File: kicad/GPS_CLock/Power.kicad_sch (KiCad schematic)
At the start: 50 parts, among them J201 USB_C_2.0, J202 BATT, Q201 PMPB17EP, Q202 PMPB17EP, U201 LP5912-3.3DRV, U202 STUSB4500QTR, U203 BQ25892, U204 TPS62827DMQ, U205 TPS62827DMQ

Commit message: updated pcb
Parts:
- removed J202: BATT, symbol Connector_Generic:Conn_01x02
- added BT201, BT202, BT203: Lipo, symbol Device:Battery_Cell
- C203, C205, C206, C212: footprint (none) -> Capacitor_SMD:C_0402_1005Metric
- C208, C209, C217, C218, C219, C221: footprint Capacitor_SMD:C_0402_1005Metric -> Capacitor_SMD:C_0603_1608Metric
- D201: footprint (none) -> Diode_SMD:D_SOD-323
- L201, L202: footprint Inductor_SMD:L_0805_2012Metric -> clock:L_DFE201610
- L203: footprint clock:Bourns_SRP2512 -> Inductor_SMD:L_Vishay_IHLP-2020
- Q201, Q202: footprint (none) -> clock:NXP_DFN6_2.0x2.0mm 2xEp
- R205: footprint (none) -> Resistor_SMD:R_0402_1005Metric
- U203: footprint (none) -> Package_DFN_QFN:Texas_S-PWQFN-N24_EP2.7x2.7mm
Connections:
- net +BATT: now also BT201.1 (+), BT202.1 (+), BT203.1 (+)
- net Earth: now also BT201.2 (-), BT202.2 (-), BT203.2 (-)
- net VBUS: now reaches D201.2 (A), J201.A4 (VBUS), J201.A9 (VBUS), J201.B4 (VBUS), J201.B9 (VBUS), Q201.1 (D), Q201.2 (D), Q201.5 (D), Q201.6 (D), Q201.7 (D), R201.1
- net VBUS_SNK: now reaches C207.1, C210.1, Q202.1 (D), Q202.2 (D), Q202.5 (D), Q202.6 (D), Q202.7 (D), U203.1 (VBUS)
- net PD_SCL: now reaches U202.7 (SCL)
- net PD_SDA: now reaches U202.8 (SDA)

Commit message: update pcb
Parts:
- C201, C220: footprint Capacitor_SMD:C_0402_1005Metric -> Capacitor_SMD:C_0603_1608Metric
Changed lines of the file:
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@@
       (effects (font (size 1.27 1.27)) (justify left))
     )
-    (property "Footprint" "Capacitor_SMD:C_0402_1005Metric" (id 2) (at 71.12 140.97 0)
+    (property "Footprint" "Capacitor_SMD:C_0603_1608Metric" (id 2) (at 71.12 140.97 0)
       (effects (font (size 1.27 1.27)) hide)
     )
@@
       (effects (font (size 1.27 1.27)) (justify left))
     )
-    (property "Footprint" "Capacitor_SMD:C_0402_1005Metric" (id 2) (at 228.6 138.43 0)
-      (effects (font (size 1.27 1.27)) hide)
-    )
+    (property "Footprint" "Capacitor_SMD:C_0603_1608Metric" (id 2) (at 228.6 138.43 0)
+      (effects (font (size 1.27 1.27)) hide)
+    )

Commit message: update pcb
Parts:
- added JP201, JP202: Jumper_2_Bridged, Connector_PinHeader_2.54mm:PinHeader_1x02_P2.54mm_Horizontal, symbol Jumper:Jumper_2_Bridged
- added R217, R218: 50, Resistor_SMD:R_1206_3216Metric, symbol Device:R_Small
- BT201, BT202, BT203: footprint (none) -> Connector_JST:JST_PH_S2B-PH-K_1x02_P2.00mm_Horizontal
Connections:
- net +BATT: now also JP201.2 (B), R217.1; no longer BT202.1 (+), BT203.1 (+)
- new net: BT202.1 (+), JP201.1 (A), JP202.2 (B), R217.2, R218.1
- new net: BT203.1 (+), JP202.1 (A), R218.2
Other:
- moved on the sheet: BT201, BT202, BT203

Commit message: update pcb
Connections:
- net PD_INT: now reaches U202.19 (ALERT)
- no-connect marks 13 -> 12

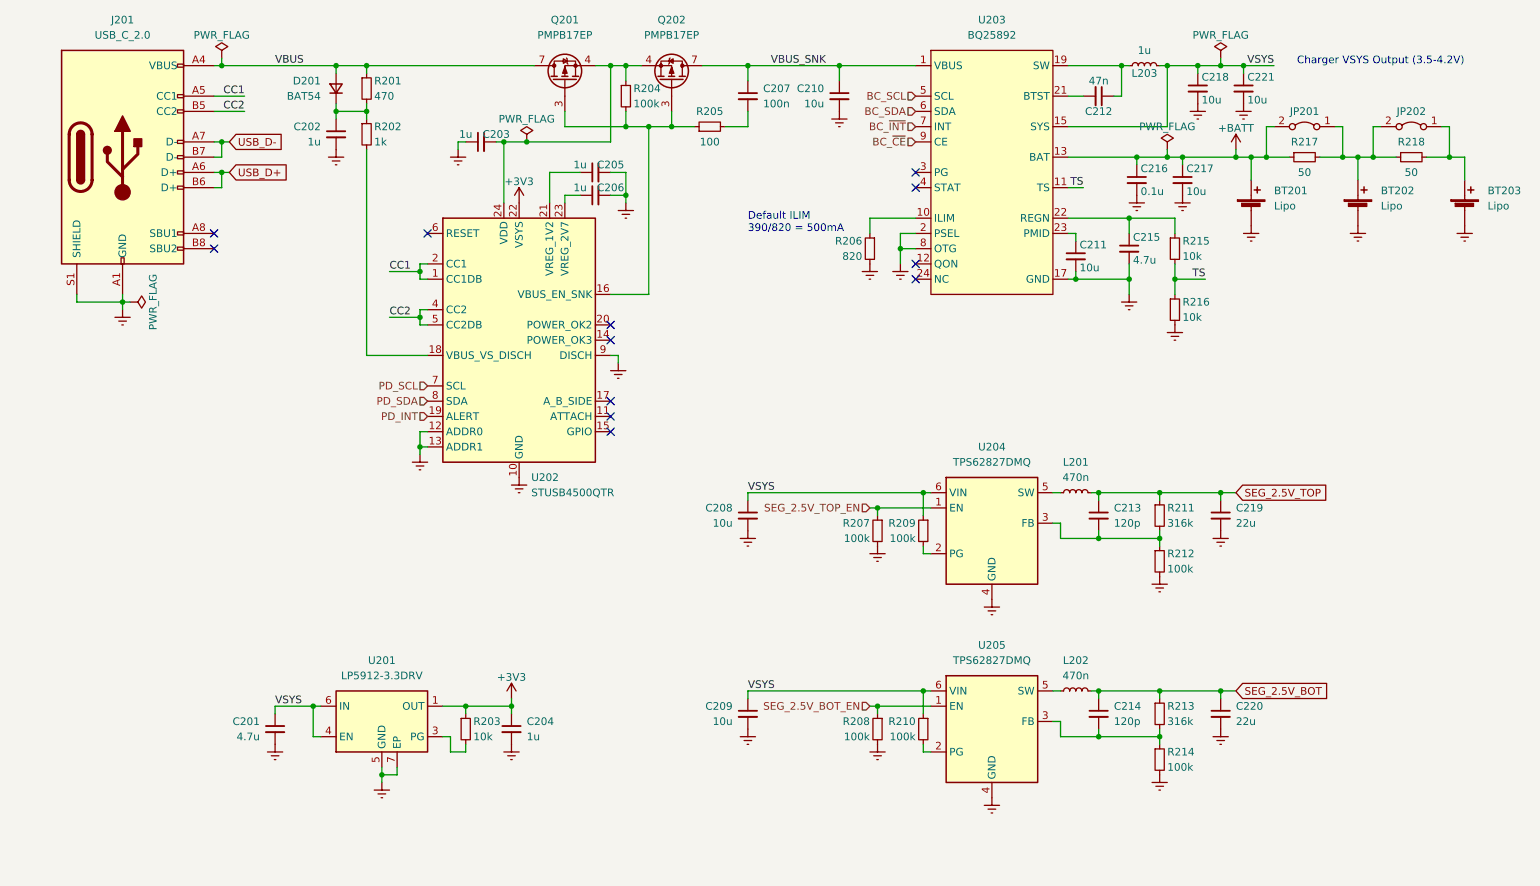
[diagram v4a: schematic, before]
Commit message: add quickcharge 3.0 capability
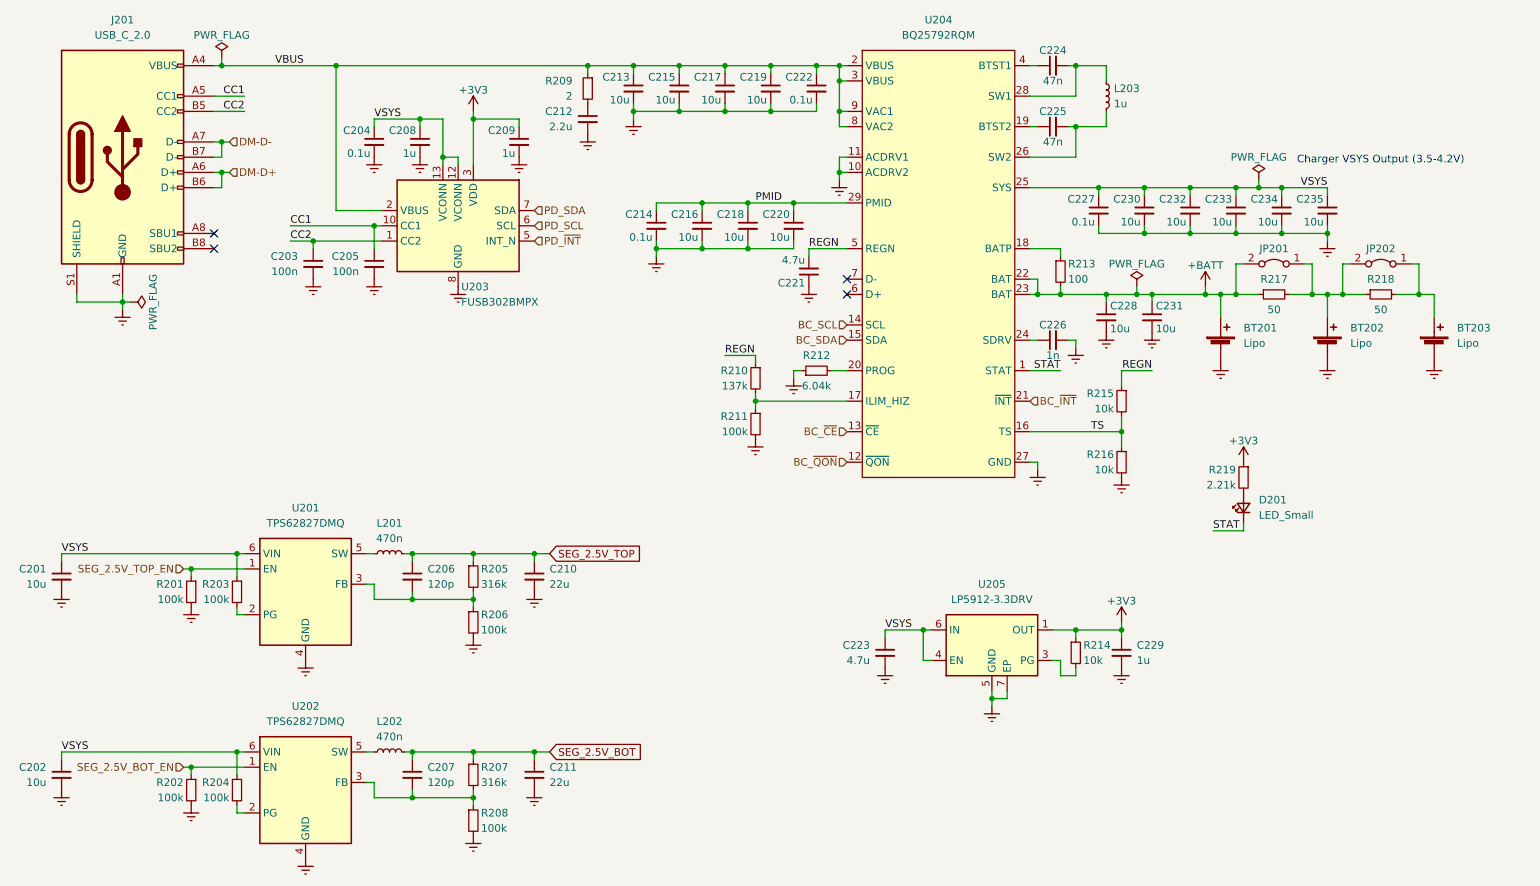
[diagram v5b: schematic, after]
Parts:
- removed C202, C206: 1u, Capacitor_SMD:C_0402_1005Metric, symbol Device:C_Small
- removed C207: 100n, Capacitor_SMD:C_0402_1005Metric, symbol Device:C_Small
- removed C211: 10u, Capacitor_SMD:C_0402_1005Metric, symbol Device:C_Small
- removed D201: BAT54, Diode_SMD:D_SOD-323, symbol Device:D_Small
- removed Q201, Q202: PMPB17EP, clock:NXP_DFN6_2.0x2.0mm 2xEp, symbol Clock:PMPB17EP
- removed R201: 470, Resistor_SMD:R_0402_1005Metric, symbol Device:R_Small
- removed R202: 1k, Resistor_SMD:R_0402_1005Metric, symbol Device:R_Small
- removed R204: 100k, Resistor_SMD:R_0402_1005Metric, symbol Device:R_Small
- removed R205: 100, Resistor_SMD:R_0402_1005Metric, symbol Device:R_Small
- removed U202: STUSB4500QTR, Package_DFN_QFN:QFN-24-1EP_4x4mm_P0.5mm_EP2.7x2.7mm, symbol Interface_USB:STUSB4500QTR
- removed U203: BQ25892, Package_DFN_QFN:Texas_S-PWQFN-N24_EP2.7x2.7mm, symbol Clock:BQ25892
- added C204, C214, C222, C227: 0.1u, Capacitor_SMD:C_0402_1005Metric, symbol Device:C_Small
- added C208, C209: 1u, Capacitor_SMD:C_0402_1005Metric, symbol Device:C_Small
- added C212: 2.2u, Capacitor_SMD:C_0402_1005Metric, symbol Device:C_Small
- added C213, C216, C217, C220: 10u, Capacitor_SMD:C_0603_1608Metric, symbol Device:C_Small
- added C225: 47n, Capacitor_SMD:C_0402_1005Metric, symbol Device:C_Small
- added C226: 1n, Capacitor_SMD:C_0402_1005Metric, symbol Device:C_Small
- added C230, C232, C233, C234, C235: 10u, Capacitor_SMD:C_0402_1005Metric, symbol Device:C_Small
- added D201: LED_Small, clock:APA1606, symbol Device:LED_Small
- added R209: 2, Resistor_SMD:R_0402_1005Metric, symbol Device:R_Small
- added R210: 137k, Resistor_SMD:R_0402_1005Metric, symbol Device:R_Small
- added R212: 6.04k, Resistor_SMD:R_0402_1005Metric, symbol Device:R_Small
- added R213: 100, Resistor_SMD:R_0402_1005Metric, symbol Device:R_Small
- added R219: 2.21k, Resistor_SMD:R_0402_1005Metric, symbol Device:R_Small
- added U203: FUSB302BMPX, Package_DFN_QFN:WQFN-14-1EP_2.5x2.5mm_P0.5mm_EP1.45x1.45mm, symbol Interface_USB:FUSB302BMPX
- added U204: BQ25792RQM, clock:VQFN-29, symbol Clock:BQ25792RQM
- C203, C205: value 1u -> 100n
- C215: value 4.7u -> 10u; footprint Capacitor_SMD:C_0402_1005Metric -> Capacitor_SMD:C_0603_1608Metric
- C219: renamed from C210; footprint Capacitor_SMD:C_0402_1005Metric -> Capacitor_SMD:C_0603_1608Metric
- C221: value 10u -> 4.7u; footprint Capacitor_SMD:C_0603_1608Metric -> Capacitor_SMD:C_0402_1005Metric
- C228: renamed from C216; value 0.1u -> 10u
- C231: renamed from C217; footprint Capacitor_SMD:C_0603_1608Metric -> Capacitor_SMD:C_0402_1005Metric
- R211: renamed from R206; value 820 -> 100k
- renumbered C208 to C201, C209 to C202, C213 to C206, C214 to C207, C219 to C210, C220 to C211, C201 to C223, C212 to C224, C204 to C229, R207 to R201, R208 to R202, R209 to R203, R210 to R204, R211 to R205, R212 to R206, R213 to R207, R214 to R208, R203 to R214, U204 to U201, U205 to U202, U201 to U205
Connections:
- net VBUS_SNK is gone; now on net VBUS: C219.1
- net +3V3: now also C209.1, R219.1, U203.3 (VDD), U203.4 (VDD)
- net +BATT: now also R213.2, U204.22 (BAT), U204.23 (BAT)
- net BC_SCL: now also U204.14 (SCL)
- net BC_SDA: now also U204.15 (SDA)
- net BC_~{CE}: now also U204.13 (~{CE})
- net BC_~{INT}: now also U204.21 (~{INT})
- net CC1: now also C205.1, U203.10 (CC1), U203.11 (CC1)
- net CC2: now also C203.1, U203.1 (CC2), U203.14 (CC2)
- net Earth: now also C203.2, C221.1, C204.2, C208.2, C209.2, C212.2, C213.2, C214.2, C216.2, C217.2, C220.2, C222.2, C226.2, C227.2, C230.2, C232.2, C233.2, C234.2, C235.2, R212.1, U203.15 (GND), U203.8 (GND), U203.9 (GND), U204.10 (ACDRV2), U204.11 (ACDRV1), U204.27 (GND); no longer C203.1, C221.2
- net PD_SCL: now also U203.6 (SCL)
- net PD_SDA: now also U203.7 (SDA)
- net TS: now also U204.16 (TS)
- net VBUS: now also C215.1, C213.1, C217.1, C222.1, R209.1, U203.2 (VBUS), U204.2 (VBUS), U204.3 (VBUS), U204.8 (VAC2), U204.9 (VAC1)
- net VSYS: now also C204.1, C208.1, C227.1, C230.1, C232.1, C233.1, C234.1, C235.1, U203.12 (VCONN), U203.13 (VCONN), U204.25 (SYS); no longer C218.1, C221.1, L203.2
- net at R211.1: now also R210.2, U204.17 (ILIM_HIZ)
- net at C224.1: now also U204.4 (BTST1); no longer L203.1
- net at C224.2: now also L203.1, U204.28 (SW1)
- net REGN: now reaches R215.1
- net REGN: now also C221.2, R210.1, U204.5 (REGN); no longer C215.1
- net USB_D+ renamed DM-D+
- net USB_D- renamed DM-D-
- new net: C225.1, U204.19 (BTST2)
- new net: C225.2, L203.2, U204.26 (SW2)
- new net: C212.1, R209.2
- new net: D201.2 (A), R219.2
- new net: C226.1, U204.24 (SDRV)
- new net: R213.1, U204.18 (BATP)
- new net: R212.2, U204.20 (PROG)
- new net BC_~{QON}: U204.12 (~{QON})
- new net PD_~{INT}: U203.5 (INT_N)
- new net PMID: C214.1, C216.1, C218.1, C220.1, U204.29 (PMID)
- new net STAT: D201.1 (K), U204.1 (STAT)
- no-connect marks 12 -> 4
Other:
- note removed: "Default ILIM 390/820 = 500mA"
- moved on the sheet: BT201, BT202, BT203, C201, C202, C206, C207, C210, C211, C219, C223, C224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

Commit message: update pcb
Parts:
- added TP201: VBUS, TestPoint:TestPoint_Bridge_Pitch2.0mm_Drill0.7mm, symbol Connector:TestPoint
- added TP202: 2V5_TOP, TestPoint:TestPoint_Bridge_Pitch2.0mm_Drill0.7mm, symbol Connector:TestPoint
- added TP203: 2.5V_BOT, TestPoint:TestPoint_Bridge_Pitch2.0mm_Drill0.7mm, symbol Connector:TestPoint
- added TP204: 3V3, TestPoint:TestPoint_Bridge_Pitch2.0mm_Drill0.7mm, symbol Connector:TestPoint
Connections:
- net +3V3: now also TP204.1
- net SEG_2.5V_BOT: now also TP203.1
- net SEG_2.5V_TOP: now also TP202.1
- net VBUS: now also TP201.1
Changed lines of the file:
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@@
   (junction (at 248.92 68.58) (diameter 0) (color 0 0 0 0)
   )
+  (junction (at 86.36 30.48) (diameter 0) (color 0 0 0 0)
+  )
   (junction (at 146.05 30.48) (diameter 0) (color 0 0 0 0)
   )
@@
   (junction (at 104.14 152.4) (diameter 0) (color 0 0 0 0)
   )
+  (junction (at 109.22 111.76) (diameter 0) (color 0 0 0 0)
+  )
   (junction (at 64.77 144.78) (diameter 0) (color 0 0 0 0)
   )
@@
   (junction (at 95.25 39.37) (diameter 0) (color 0 0 0 0)
   )
+  (junction (at 109.22 144.78) (diameter 0) (color 0 0 0 0)
+  )
   (junction (at 165.1 38.1) (diameter 0) (color 0 0 0 0)
   )
@@
   )
   (junction (at 246.38 68.58) (diameter 0) (color 0 0 0 0)
+  )
+  (junction (at 201.93 124.46) (diameter 0) (color 0 0 0 0)
   )
   (junction (at 209.55 68.58) (diameter 0) (color 0 0 0 0)
@@
     (stroke (width 0) (type default) (color 0 0 0 0))
   )
+  (wire (pts (xy 201.93 123.19) (xy 201.93 124.46))
+    (stroke (width 0) (type default) (color 0 0 0 0))
+  )
   (wire (pts (xy 111.76 39.37) (xy 104.14 39.37))
     (stroke (width 0) (type default) (color 0 0 0 0))
@@
     (stroke (width 0) (type default) (color 0 0 0 0))
   )
-  (wire (pts (xy 204.47 124.46) (xy 200.66 124.46))
+  (wire (pts (xy 204.47 124.46) (xy 201.93 124.46))
     (stroke (width 0) (type default) (color 0 0 0 0))
   )
@@
     (stroke (width 0) (type default) (color 0 0 0 0))
   )
-  (wire (pts (xy 114.3 144.78) (xy 104.14 144.78))
+  (wire (pts (xy 114.3 144.78) (xy 109.22 144.78))
     (stroke (width 0) (type default) (color 0 0 0 0))
   )
@@
     (stroke (width 0) (type default) (color 0 0 0 0))
   )
+  (wire (pts (xy 86.36 30.48) (xy 123.19 30.48))
+    (stroke (width 0) (type default) (color 0 0 0 0))
+  )
   (wire (pts (xy 196.85 81.28) (xy 201.93 81.28))
     (stroke (width 0) (type default) (color 0 0 0 0))
@@
     (stroke (width 0) (type default) (color 0 0 0 0))
   )
-  (wire (pts (xy 114.3 111.76) (xy 104.14 111.76))
+  (wire (pts (xy 114.3 111.76) (xy 109.22 111.76))
+    (stroke (width 0) (type default) (color 0 0 0 0))
+  )
+  (wire (pts (xy 109.22 144.78) (xy 104.14 144.78))
     (stroke (width 0) (type default) (color 0 0 0 0))
   )
@@
     (stroke (width 0) (type default) (color 0 0 0 0))
   )
+  (wire (pts (xy 86.36 29.21) (xy 86.36 30.48))
+    (stroke (width 0) (type default) (color 0 0 0 0))
+  )
   (wire (pts (xy 234.95 50.8) (xy 238.76 50.8))
     (stroke (width 0) (type default) (color 0 0 0 0))
@@
     (stroke (width 0) (type default) (color 0 0 0 0))
   )
+  (wire (pts (xy 109.22 111.76) (xy 104.14 111.76))
+    (stroke (width 0) (type default) (color 0 0 0 0))
+  )
   (wire (pts (xy 234.95 49.53) (xy 234.95 50.8))
     (stroke (width 0) (type default) (color 0 0 0 0))
@@
     (stroke (width 0) (type default) (color 0 0 0 0))
   )
+  (wire (pts (xy 109.22 110.49) (xy 109.22 111.76))
+    (stroke (width 0) (type default) (color 0 0 0 0))
+  )
   (wire (pts (xy 64.77 144.78) (xy 66.04 144.78))
     (stroke (width 0) (type default) (color 0 0 0 0))
@@
     (stroke (width 0) (type default) (color 0 0 0 0))
   )
+  (wire (pts (xy 109.22 143.51) (xy 109.22 144.78))
+    (stroke (width 0) (type default) (color 0 0 0 0))
+  )
   (wire (pts (xy 64.77 144.78) (xy 64.77 148.59))
     (stroke (width 0) (type default) (color 0 0 0 0))
@@
     (stroke (width 0) (type default) (color 0 0 0 0))
   )
+  (wire (pts (xy 201.93 124.46) (xy 200.66 124.46))
+    (stroke (width 0) (type default) (color 0 0 0 0))
+  )
   (wire (pts (xy 57.15 114.3) (xy 66.04 114.3))
     (stroke (width 0) (type default) (color 0 0 0 0))
@@
     (stroke (width 0) (type default) (color 0 0 0 0))
   )
-  (wire (pts (xy 81.28 30.48) (xy 123.19 30.48))
+  (wire (pts (xy 81.28 30.48) (xy 86.36 30.48))
     (stroke (width 0) (type default) (color 0 0 0 0))
   )
@@
     (pin "1")
     (pin "2")
+  )
+  (symbol (lib_id "Connector:TestPoint") (at 109.22 143.51 0) (unit 1)
+    (in_bom yes) (on_board yes) (fields_autoplaced)
+    (property "Reference" "TP203" (id 0) (at 111.76 138.9379 0)
+      (effects (font (size 1.27 1.27)) (justify left))
+    )
+    (property "Value" "2.5V_BOT" (id 1) (at 111.76 141.4779 0)
+      (effects (font (size 1.27 1.27)) (justify left))
+    )
+    (property "Footprint" "TestPoint:TestPoint_Bridge_Pitch2.0mm_Drill0.7mm" (id 2) (at 114.3 143.51 0)
+      (effects (font (size 1.27 1.27)) hide)
+    )
+    (property "Datasheet" "~" (id 3) (at 114.3 143.51 0)
+      (effects (font (size 1.27 1.27)) hide)
+    )
+    (pin "1")
   )
   (symbol (lib_id "Interface_USB:FUSB302BMPX") (at 101.6 57.15 0) (mirror y) (unit 1)
@@
     (pin "2")
   )
+  (symbol (lib_id "Connector:TestPoint") (at 86.36 29.21 0) (unit 1)
+    (in_bom yes) (on_board yes) (fields_autoplaced)
+    (property "Reference" "TP201" (id 0) (at 88.9 24.6379 0)
+      (effects (font (size 1.27 1.27)) (justify left))
+    )
+    (property "Value" "VBUS" (id 1) (at 88.9 27.1779 0)
+      (effects (font (size 1.27 1.27)) (justify left))
+    )
+    (property "Footprint" "TestPoint:TestPoint_Bridge_Pitch2.0mm_Drill0.7mm" (id 2) (at 91.44 29.21 0)
+      (effects (font (size 1.27 1.27)) hide)
+    )
+    (property "Datasheet" "~" (id 3) (at 91.44 29.21 0)
+      (effects (font (size 1.27 1.27)) hide)
+    )
+    (pin "1")
+  )
   (symbol (lib_id "Device:C_Small") (at 160.02 64.77 180) (unit 1)
     (in_bom yes) (on_board yes)
@@
       (effects (font (size 1.27 1.27)) hide)
     )
+    (pin "1")
+  )
+  (symbol (lib_id "Connector:TestPoint") (at 201.93 123.19 0) (unit 1)
+    (in_bom yes) (on_board yes) (fields_autoplaced)
+    (property "Reference" "TP204" (id 0) (at 204.47 118.6179 0)
+      (effects (font (size 1.27 1.27)) (justify left))
+    )
+    (property "Value" "3V3" (id 1) (at 204.47 121.1579 0)
+      (effects (font (size 1.27 1.27)) (justify left))
+    )
+    (property "Footprint" "TestPoint:TestPoint_Bridge_Pitch2.0mm_Drill0.7mm" (id 2) (at 207.01 123.19 0)
+      (effects (font (size 1.27 1.27)) hide)
+    )
+    (property "Datasheet" "~" (id 3) (at 207.01 123.19 0)
+      (effects (font (size 1.27 1.27)) hide)
+    )
+    (pin "1")
+  )
+  (symbol (lib_id "Connector:TestPoint") (at 109.22 110.49 0) (unit 1)
+    (in_bom yes) (on_board yes) (fields_autoplaced)
+    (property "Reference" "TP202" (id 0) (at 111.76 105.9179 0)
+      (effects (font (size 1.27 1.27)) (justify left))
+    )
+    (property "Value" "2V5_TOP" (id 1) (at 111.76 108.4579 0)
+      (effects (font (size 1.27 1.27)) (justify left))
+    )
+    (property "Footprint" "TestPoint:TestPoint_Bridge_Pitch2.0mm_Drill0.7mm" (id 2) (at 114.3 110.49 0)
+      (effects (font (size 1.27 1.27)) hide)
+    )
+    (property "Datasheet" "~" (id 3) (at 114.3 110.49 0)
+      (effects (font (size 1.27 1.27)) hide)
+    )

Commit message: update pcb
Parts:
- removed TP204: 3V3, TestPoint:TestPoint_Bridge_Pitch2.0mm_Drill0.7mm, symbol Connector:TestPoint
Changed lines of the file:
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@@
   (junction (at 246.38 68.58) (diameter 0) (color 0 0 0 0)
-  )
-  (junction (at 201.93 124.46) (diameter 0) (color 0 0 0 0)
   )
   (junction (at 209.55 68.58) (diameter 0) (color 0 0 0 0)
@@
     (stroke (width 0) (type default) (color 0 0 0 0))
   )
-  (wire (pts (xy 201.93 123.19) (xy 201.93 124.46))
-    (stroke (width 0) (type default) (color 0 0 0 0))
-  )
   (wire (pts (xy 111.76 39.37) (xy 104.14 39.37))
     (stroke (width 0) (type default) (color 0 0 0 0))
@@
     (stroke (width 0) (type default) (color 0 0 0 0))
   )
-  (wire (pts (xy 204.47 124.46) (xy 201.93 124.46))
-    (stroke (width 0) (type default) (color 0 0 0 0))
-  )
   (wire (pts (xy 45.72 69.85) (xy 45.72 68.58))
     (stroke (width 0) (type default) (color 0 0 0 0))
@@
     (stroke (width 0) (type default) (color 0 0 0 0))
   )
-  (wire (pts (xy 201.93 124.46) (xy 200.66 124.46))
+  (wire (pts (xy 200.66 124.46) (xy 204.47 124.46))
     (stroke (width 0) (type default) (color 0 0 0 0))
   )
@@
       (effects (font (size 1.27 1.27)) hide)
     )
-    (pin "1")
-  )
-  (symbol (lib_id "Connector:TestPoint") (at 201.93 123.19 0) (unit 1)
-    (in_bom yes) (on_board yes) (fields_autoplaced)
-    (property "Reference" "TP204" (id 0) (at 204.47 118.6179 0)
-      (effects (font (size 1.27 1.27)) (justify left))
-    )
-    (property "Value" "3V3" (id 1) (at 204.47 121.1579 0)
-      (effects (font (size 1.27 1.27)) (justify left))
-    )
-    (property "Footprint" "TestPoint:TestPoint_Bridge_Pitch2.0mm_Drill0.7mm" (id 2) (at 207.01 123.19 0)
-      (effects (font (size 1.27 1.27)) hide)
-    )
-    (property "Datasheet" "~" (id 3) (at 207.01 123.19 0)
-      (effects (font (size 1.27 1.27)) hide)
-    )
